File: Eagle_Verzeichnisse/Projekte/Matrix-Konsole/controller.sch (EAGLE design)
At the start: 14 parts, among them IC1 74HC165D

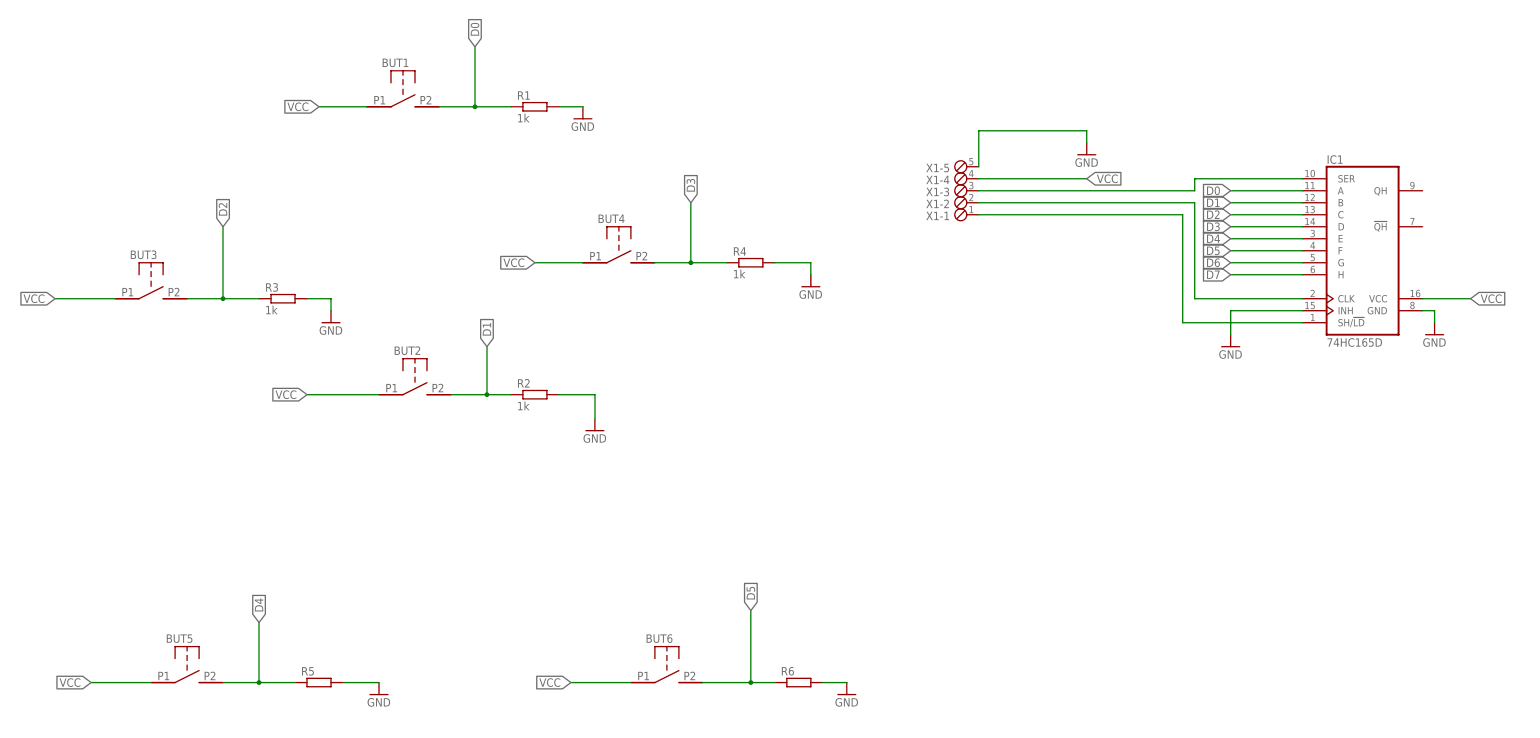
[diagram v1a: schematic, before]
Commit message: Added MAX7219 Library
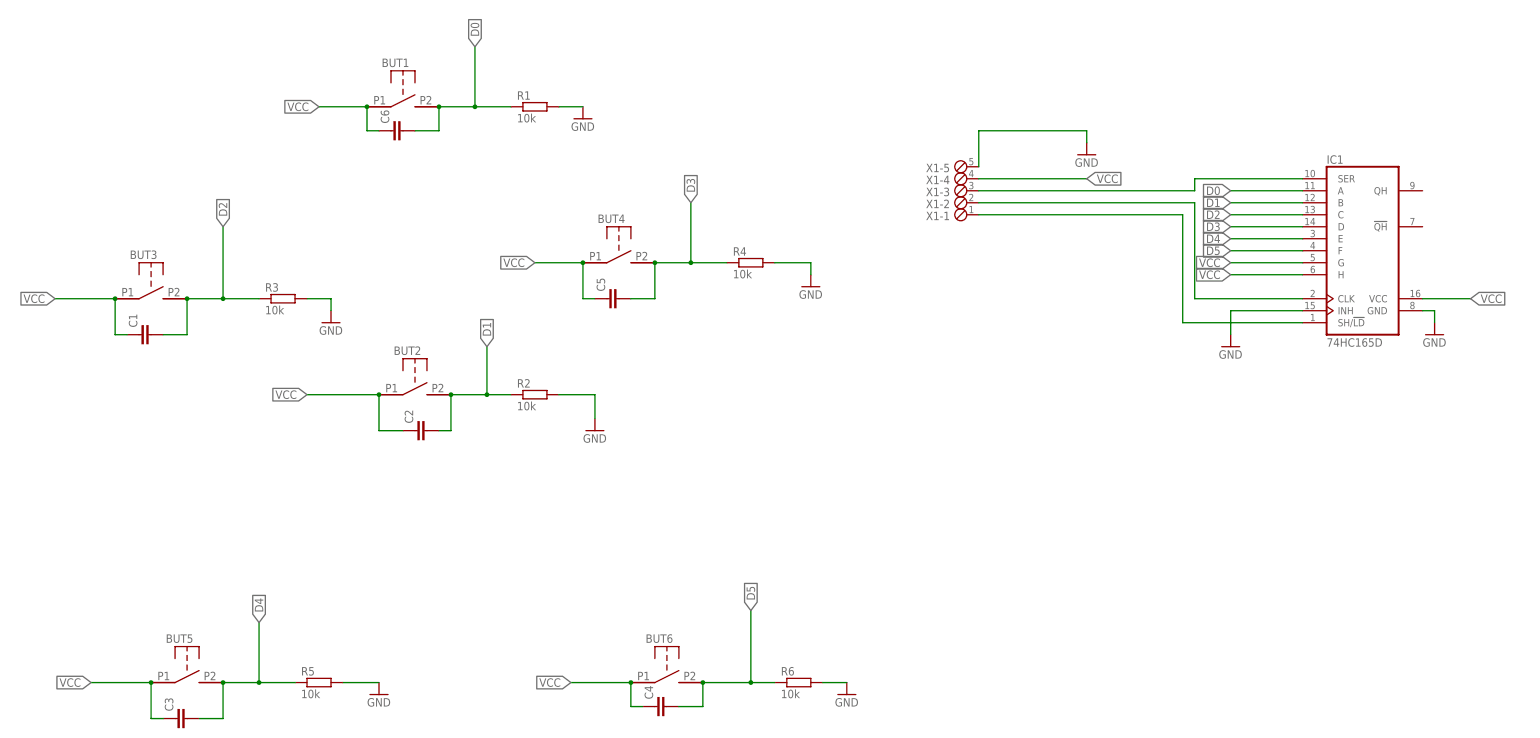
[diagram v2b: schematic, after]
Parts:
- added C1, C2, C3, C4, C5, C6: (no value), eagle-ltspice:C
- R1, R2, R3, R4: value 1k -> 10k
- R5, R6: value (none) -> 10k
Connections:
- removed net D6: IC1.G
- removed net D7: IC1.H
- net D0: now also C6.2
- net D1: now also C2.2
- net D2: now also C1.2
- net D3: now also C5.2
- net D4: now also C3.2
- net D5: now also C4.2
- net VCC: now also C1.1, C2.1, C3.1, C4.1, C5.1, C6.1, IC1.G, IC1.H
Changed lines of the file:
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@@
 <part name="BUT5" library="button" deviceset="BUTTON_DEV" device=""/>
 <part name="BUT6" library="button" deviceset="BUTTON_DEV" device=""/>
-<part name="R1" library="resistor" deviceset="R-EU_" device="0414/5V" value="1k"/>
-<part name="R2" library="resistor" deviceset="R-EU_" device="0414/5V" value="1k"/>
-<part name="R3" library="resistor" deviceset="R-EU_" device="0414/5V" value="1k"/>
-<part name="R4" library="resistor" deviceset="R-EU_" device="0414/5V" value="1k"/>
-<part name="R5" library="resistor" deviceset="R-EU_" device="0414/5V"/>
-<part name="R6" library="resistor" deviceset="R-EU_" device="0414/5V"/>
+<part name="R1" library="resistor" deviceset="R-EU_" device="0414/5V" value="10k"/>
+<part name="R2" library="resistor" deviceset="R-EU_" device="0414/5V" value="10k"/>
+<part name="R3" library="resistor" deviceset="R-EU_" device="0414/5V" value="10k"/>
+<part name="R4" library="resistor" deviceset="R-EU_" device="0414/5V" value="10k"/>
+<part name="R5" library="resistor" deviceset="R-EU_" device="0414/5V" value="10k"/>
+<part name="R6" library="resistor" deviceset="R-EU_" device="0414/5V" value="10k"/>
 <part name="IC1" library="74xx-eu" deviceset="74*165" device="D" technology="HC"/>
 <part name="GND1" library="supply1" deviceset="GND" device=""/>
@@
 <part name="X1" library="con-phoenix-254" deviceset="MPT5" device=""/>
 <part name="GND9" library="supply1" deviceset="GND" device=""/>
+<part name="C1" library="eagle-ltspice" deviceset="C" device=""/>
+<part name="C2" library="eagle-ltspice" deviceset="C" device=""/>
+<part name="C3" library="eagle-ltspice" deviceset="C" device=""/>
+<part name="C4" library="eagle-ltspice" deviceset="C" device=""/>
+<part name="C5" library="eagle-ltspice" deviceset="C" device=""/>
+<part name="C6" library="eagle-ltspice" deviceset="C" device=""/>
 </parts>
 <sheets>
@@
 <instance part="X1" gate="-5" x="-60.96" y="60.96" rot="R180"/>
 <instance part="GND9" gate="1" x="-35.56" y="63.5"/>
+<instance part="C1" gate="G$1" x="-236.22" y="25.4" rot="R90"/>
+<instance part="C2" gate="G$1" x="-177.8" y="5.08" rot="R90"/>
+<instance part="C3" gate="G$1" x="-228.6" y="-55.88" rot="R90"/>
+<instance part="C4" gate="G$1" x="-127" y="-53.34" rot="R90"/>
+<instance part="C5" gate="G$1" x="-137.16" y="33.02" rot="R90"/>
+<instance part="C6" gate="G$1" x="-182.88" y="68.58" rot="R90"/>
 </instances>
 <busses>
@@
 <wire x1="-187.96" y1="73.66" x2="-198.12" y2="73.66" width="0.1524" layer="91"/>
 <label x="-198.12" y="73.66" size="1.778" layer="95" rot="R180" xref="yes"/>
+<pinref part="C6" gate="G$1" pin="1"/>
+<wire x1="-185.42" y1="68.58" x2="-187.96" y2="68.58" width="0.1524" layer="91"/>
+<wire x1="-187.96" y1="68.58" x2="-187.96" y2="73.66" width="0.1524" layer="91"/>
+<junction x="-187.96" y="73.66"/>
 </segment>
 <segment>
@@
 <wire x1="-142.24" y1="40.64" x2="-152.4" y2="40.64" width="0.1524" layer="91"/>
 <label x="-152.4" y="40.64" size="1.778" layer="95" rot="R180" xref="yes"/>
+<pinref part="C5" gate="G$1" pin="1"/>
+<wire x1="-139.7" y1="33.02" x2="-142.24" y2="33.02" width="0.1524" layer="91"/>
+<wire x1="-142.24" y1="33.02" x2="-142.24" y2="40.64" width="0.1524" layer="91"/>
+<junction x="-142.24" y="40.64"/>
 </segment>
 <segment>
@@
 <wire x1="-241.3" y1="33.02" x2="-254" y2="33.02" width="0.1524" layer="91"/>
 <label x="-254" y="33.02" size="1.778" layer="95" rot="R180" xref="yes"/>
+<pinref part="C1" gate="G$1" pin="1"/>
+<wire x1="-238.76" y1="25.4" x2="-241.3" y2="25.4" width="0.1524" layer="91"/>
+<wire x1="-241.3" y1="25.4" x2="-241.3" y2="33.02" width="0.1524" layer="91"/>
+<junction x="-241.3" y="33.02"/>
 </segment>
 <segment>
@@
 <wire x1="-185.42" y1="12.7" x2="-200.66" y2="12.7" width="0.1524" layer="91"/>
 <label x="-200.66" y="12.7" size="1.778" layer="95" rot="R180" xref="yes"/>
+<pinref part="C2" gate="G$1" pin="1"/>
+<wire x1="-180.34" y1="5.08" x2="-185.42" y2="5.08" width="0.1524" layer="91"/>
+<wire x1="-185.42" y1="5.08" x2="-185.42" y2="12.7" width="0.1524" layer="91"/>
+<junction x="-185.42" y="12.7"/>
 </segment>
 <segment>
@@
 <wire x1="-233.68" y1="-48.26" x2="-246.38" y2="-48.26" width="0.1524" layer="91"/>
 <label x="-246.38" y="-48.26" size="1.778" layer="95" rot="R180" xref="yes"/>
+<pinref part="C3" gate="G$1" pin="1"/>
+<wire x1="-231.14" y1="-55.88" x2="-233.68" y2="-55.88" width="0.1524" layer="91"/>
+<wire x1="-233.68" y1="-55.88" x2="-233.68" y2="-48.26" width="0.1524" layer="91"/>
+<junction x="-233.68" y="-48.26"/>
 </segment>
 <segment>
@@
 <wire x1="-132.08" y1="-48.26" x2="-144.78" y2="-48.26" width="0.1524" layer="91"/>
 <label x="-144.78" y="-48.26" size="1.778" layer="95" rot="R180" xref="yes"/>
+<pinref part="C4" gate="G$1" pin="1"/>
+<wire x1="-129.54" y1="-53.34" x2="-132.08" y2="-53.34" width="0.1524" layer="91"/>
+<wire x1="-132.08" y1="-53.34" x2="-132.08" y2="-48.26" width="0.1524" layer="91"/>
+<junction x="-132.08" y="-48.26"/>
 </segment>
 <segment>
@@
 <wire x1="-58.42" y1="58.42" x2="-35.56" y2="58.42" width="0.1524" layer="91"/>
 <label x="-35.56" y="58.42" size="1.778" layer="95" xref="yes"/>
+</segment>
+<segment>
+<pinref part="IC1" gate="A" pin="G"/>
+<wire x1="10.16" y1="40.64" x2="-5.08" y2="40.64" width="0.1524" layer="91"/>
+<label x="-5.08" y="40.64" size="1.778" layer="95" rot="R180" xref="yes"/>
+</segment>
+<segment>
+<pinref part="IC1" gate="A" pin="H"/>
+<wire x1="10.16" y1="38.1" x2="-5.08" y2="38.1" width="0.1524" layer="91"/>
+<label x="-5.08" y="38.1" size="1.778" layer="95" rot="R180" xref="yes"/>
 </segment>
 </net>
@@
 <wire x1="-165.1" y1="73.66" x2="-165.1" y2="86.36" width="0.1524" layer="91"/>
 <label x="-165.1" y="86.36" size="1.778" layer="95" rot="R90" xref="yes"/>
+<pinref part="C6" gate="G$1" pin="2"/>
+<wire x1="-177.8" y1="68.58" x2="-172.72" y2="68.58" width="0.1524" layer="91"/>
+<wire x1="-172.72" y1="68.58" x2="-172.72" y2="73.66" width="0.1524" layer="91"/>
+<junction x="-172.72" y="73.66"/>
 </segment>
 </net>
@@
 <wire x1="-162.56" y1="12.7" x2="-162.56" y2="22.86" width="0.1524" layer="91"/>
 <label x="-162.56" y="22.86" size="1.778" layer="95" rot="R90" xref="yes"/>
+<pinref part="C2" gate="G$1" pin="2"/>
+<wire x1="-172.72" y1="5.08" x2="-170.18" y2="5.08" width="0.1524" layer="91"/>
+<wire x1="-170.18" y1="5.08" x2="-170.18" y2="12.7" width="0.1524" layer="91"/>
+<junction x="-170.18" y="12.7"/>
 </segment>
 </net>
@@
 <wire x1="-218.44" y1="33.02" x2="-218.44" y2="48.26" width="0.1524" layer="91"/>
 <label x="-218.44" y="48.26" size="1.778" layer="95" rot="R90" xref="yes"/>
+<pinref part="C1" gate="G$1" pin="2"/>
+<wire x1="-231.14" y1="25.4" x2="-226.06" y2="25.4" width="0.1524" layer="91"/>
+<wire x1="-226.06" y1="25.4" x2="-226.06" y2="33.02" width="0.1524" layer="91"/>
+<junction x="-226.06" y="33.02"/>
 </segment>
 </net>
@@
 <wire x1="-119.38" y1="40.64" x2="-119.38" y2="53.34" width="0.1524" layer="91"/>
 <label x="-119.38" y="53.34" size="1.778" layer="95" rot="R90" xref="yes"/>
+<pinref part="C5" gate="G$1" pin="2"/>
+<wire x1="-132.08" y1="33.02" x2="-127" y2="33.02" width="0.1524" layer="91"/>
+<wire x1="-127" y1="33.02" x2="-127" y2="40.64" width="0.1524" layer="91"/>
+<junction x="-127" y="40.64"/>
 </segment>
 </net>
@@
 <wire x1="-210.82" y1="-48.26" x2="-210.82" y2="-35.56" width="0.1524" layer="91"/>
 <label x="-210.82" y="-35.56" size="1.778" layer="95" rot="R90" xref="yes"/>
+<pinref part="C3" gate="G$1" pin="2"/>
+<wire x1="-223.52" y1="-55.88" x2="-218.44" y2="-55.88" width="0.1524" layer="91"/>
+<wire x1="-218.44" y1="-55.88" x2="-218.44" y2="-48.26" width="0.1524" layer="91"/>
+<junction x="-218.44" y="-48.26"/>
 </segment>
 </net>
@@
 <wire x1="-106.68" y1="-48.26" x2="-106.68" y2="-33.02" width="0.1524" layer="91"/>
 <label x="-106.68" y="-33.02" size="1.778" layer="95" rot="R90" xref="yes"/>
-</segment>
-</net>
-<net name="D6" class="0">
-<segment>
-<pinref part="IC1" gate="A" pin="G"/>
-<wire x1="10.16" y1="40.64" x2="-5.08" y2="40.64" width="0.1524" layer="91"/>
-<label x="-5.08" y="40.64" size="1.778" layer="95" rot="R180" xref="yes"/>
-</segment>
-</net>
-<net name="D7" class="0">
-<segment>
-<pinref part="IC1" gate="A" pin="H"/>
-<wire x1="10.16" y1="38.1" x2="-5.08" y2="38.1" width="0.1524" layer="91"/>
-<label x="-5.08" y="38.1" size="1.778" layer="95" rot="R180" xref="yes"/>
-</segment>
-</net>
+<pinref part="C4" gate="G$1" pin="2"/>
+<wire x1="-121.92" y1="-53.34" x2="-116.84" y2="-53.34" width="0.1524" layer="91"/>
+<wire x1="-116.84" y1="-53.34" x2="-116.84" y2="-48.26" width="0.1524" layer="91"/>
+<junction x="-116.84" y="-48.26"/>
+</segment>
+</net>
